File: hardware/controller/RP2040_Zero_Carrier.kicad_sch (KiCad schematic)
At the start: 2 parts, among them J1 20P 1.0mm FFC Type A, U1 Waveshare RP2040-Zero 23.5x18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

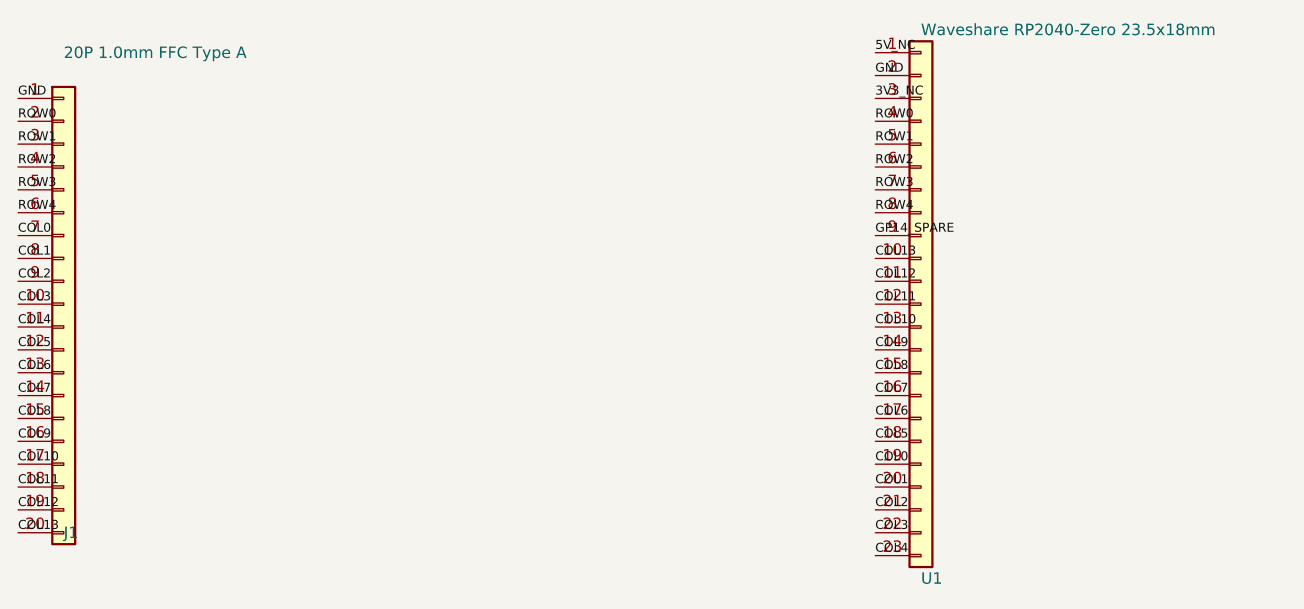
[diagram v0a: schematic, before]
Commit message: Finalize FFC routing and assembly-safe hardware
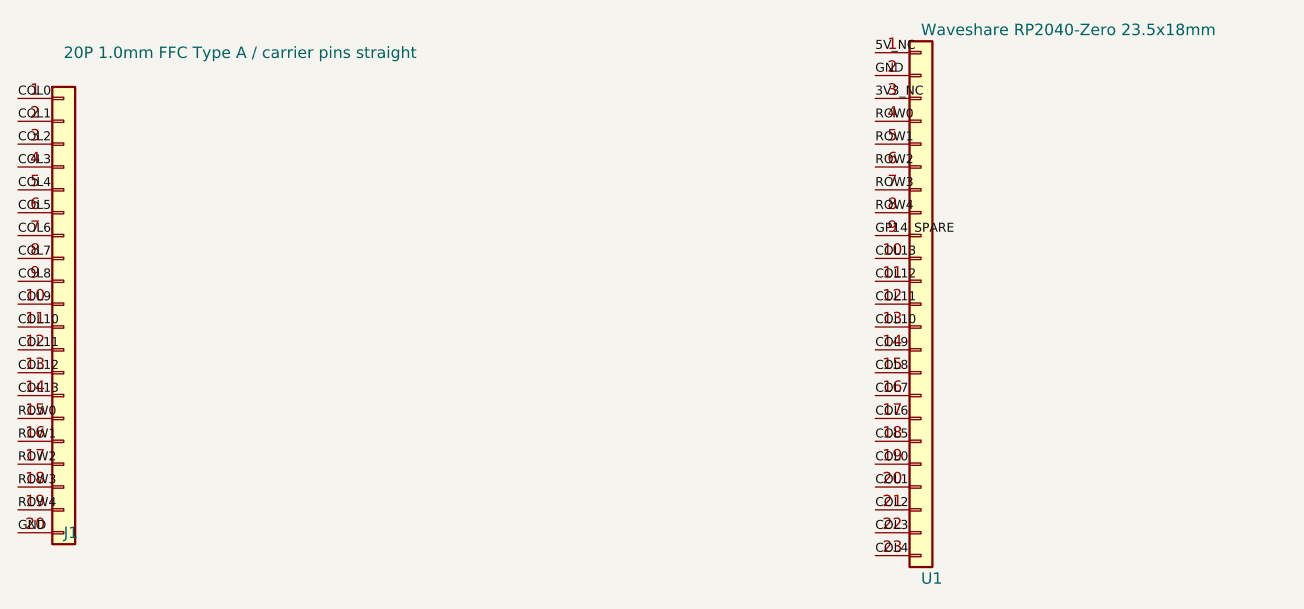
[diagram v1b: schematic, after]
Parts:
- J1: value 20P 1.0mm FFC Type A -> 20P 1.0mm FFC Type A / carrier pins straight
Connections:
- net COL0: now also J1.1 (Pin_1); no longer J1.7 (Pin_7)
- net COL1: now also J1.2 (Pin_2); no longer J1.8 (Pin_8)
- net COL10: now also J1.11 (Pin_11); no longer J1.17 (Pin_17)
- net COL11: now also J1.12 (Pin_12); no longer J1.18 (Pin_18)
- net COL12: now also J1.13 (Pin_13); no longer J1.19 (Pin_19)
- net COL13: now also J1.14 (Pin_14); no longer J1.20 (Pin_20)
- net COL2: now also J1.3 (Pin_3); no longer J1.9 (Pin_9)
- net COL3: now also J1.4 (Pin_4); no longer J1.10 (Pin_10)
- net COL4: now also J1.5 (Pin_5); no longer J1.11 (Pin_11)
- net COL5: now also J1.6 (Pin_6); no longer J1.12 (Pin_12)
- net COL6: now also J1.7 (Pin_7); no longer J1.13 (Pin_13)
- net COL7: now also J1.8 (Pin_8); no longer J1.14 (Pin_14)
- net COL8: now also J1.9 (Pin_9); no longer J1.15 (Pin_15)
- net COL9: now also J1.10 (Pin_10); no longer J1.16 (Pin_16)
- net GND: now also J1.20 (Pin_20); no longer J1.1 (Pin_1)
- net ROW0: now also J1.15 (Pin_15); no longer J1.2 (Pin_2)
- net ROW1: now also J1.16 (Pin_16); no longer J1.3 (Pin_3)
- net ROW2: now also J1.17 (Pin_17); no longer J1.4 (Pin_4)
- net ROW3: now also J1.18 (Pin_18); no longer J1.5 (Pin_5)
- net ROW4: now also J1.19 (Pin_19); no longer J1.6 (Pin_6)
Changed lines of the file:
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@@
 			)
 		)
-		(property "Value" "20P 1.0mm FFC Type A"
+		(property "Value" "20P 1.0mm FFC Type A / carrier pins straight"
 			(at 44.45 72.39 0.0000)
 			(effects
@@
 		(instances
 			(project "Minilite64 RP2040-Zero carrier"
-				(path "/281aadff-97dc-4c5d-822a-491d4e866b42"
+				(path "/44f8c00c-14ab-4b52-8662-688700ab1df1"
 					(reference "J1")
 					(unit 1)
@@
 		(instances
 			(project "Minilite64 RP2040-Zero carrier"
-				(path "/281aadff-97dc-4c5d-822a-491d4e866b42"
+				(path "/44f8c00c-14ab-4b52-8662-688700ab1df1"
 					(reference "U1")
 					(unit 1)
@@
 		)
 	)
+	(label "COL0"
+		(at 39.37 77.47 180)
+		(effects
+			(font
+				(size 1 1)
+			)
+			(justify left bottom)
+		)
+	)
+	(label "COL1"
+		(at 39.37 80.01 180)
+		(effects
+			(font
+				(size 1 1)
+			)
+			(justify left bottom)
+		)
+	)
+	(label "COL2"
+		(at 39.37 82.55 180)
+		(effects
+			(font
+				(size 1 1)
+			)
+			(justify left bottom)
+		)
+	)
+	(label "COL3"
+		(at 39.37 85.09 180)
+		(effects
+			(font
+				(size 1 1)
+			)
+			(justify left bottom)
+		)
+	)
+	(label "COL4"
+		(at 39.37 87.63 180)
+		(effects
+			(font
+				(size 1 1)
+			)
+			(justify left bottom)
+		)
+	)
+	(label "COL5"
+		(at 39.37 90.17 180)
+		(effects
+			(font
+				(size 1 1)
+			)
+			(justify left bottom)
+		)
+	)
+	(label "COL6"
+		(at 39.37 92.71 180)
+		(effects
+			(font
+				(size 1 1)
+			)
+			(justify left bottom)
+		)
+	)
+	(label "COL7"
+		(at 39.37 95.25 180)
+		(effects
+			(font
+				(size 1 1)
+			)
+			(justify left bottom)
+		)
+	)
+	(label "COL8"
+		(at 39.37 97.79 180)
+		(effects
+			(font
+				(size 1 1)
+			)
+			(justify left bottom)
+		)
+	)
+	(label "COL9"
+		(at 39.37 100.33 180)
+		(effects
+			(font
+				(size 1 1)
+			)
+			(justify left bottom)
+		)
+	)
+	(label "COL10"
+		(at 39.37 102.87 180)
+		(effects
+			(font
+				(size 1 1)
+			)
+			(justify left bottom)
+		)
+	)
+	(label "COL11"
+		(at 39.37 105.41 180)
+		(effects
+			(font
+				(size 1 1)
+			)
+			(justify left bottom)
+		)
+	)
+	(label "COL12"
+		(at 39.37 107.95 180)
+		(effects
+			(font
+				(size 1 1)
+			)
+			(justify left bottom)
+		)
+	)
+	(label "COL13"
+		(at 39.37 110.49 180)
+		(effects
+			(font
+				(size 1 1)
+			)
+			(justify left bottom)
+		)
+	)
+	(label "ROW0"
+		(at 39.37 113.03 180)
+		(effects
+			(font
+				(size 1 1)
+			)
+			(justify left bottom)
+		)
+	)
+	(label "ROW1"
+		(at 39.37 115.57 180)
+		(effects
+			(font
+				(size 1 1)
+			)
+			(justify left bottom)
+		)
+	)
+	(label "ROW2"
+		(at 39.37 118.11 180)
+		(effects
+			(font
+				(size 1 1)
+			)
+			(justify left bottom)
+		)
+	)
+	(label "ROW3"
+		(at 39.37 120.65 180)
+		(effects
+			(font
+				(size 1 1)
+			)
+			(justify left bottom)
+		)
+	)
+	(label "ROW4"
+		(at 39.37 123.19 180)
+		(effects
+			(font
+				(size 1 1)
+			)
+			(justify left bottom)
+		)
+	)
 	(label "GND"
-		(at 39.37 77.47 180)
-		(effects
-			(font
-				(size 1 1)
-			)
-			(justify left bottom)
-		)
-	)
-	(label "ROW0"
-		(at 39.37 80.01 180)
-		(effects
-			(font
-				(size 1 1)
-			)
-			(justify left bottom)
-		)
-	)
-	(label "ROW1"
-		(at 39.37 82.55 180)
-		(effects
-			(font
-				(size 1 1)
-			)
-			(justify left bottom)
-		)
-	)
-	(label "ROW2"
-		(at 39.37 85.09 180)
-		(effects
-			(font
-				(size 1 1)
-			)
-			(justify left bottom)
-		)
-	)
-	(label "ROW3"
-		(at 39.37 87.63 180)
-		(effects
-			(font
-				(size 1 1)
-			)
-			(justify left bottom)
-		)
-	)
-	(label "ROW4"
-		(at 39.37 90.17 180)
-		(effects
-			(font
-				(size 1 1)
-			)
-			(justify left bottom)
-		)
-	)
-	(label "COL0"
-		(at 39.37 92.71 180)
-		(effects
-			(font
-				(size 1 1)
-			)
-			(justify left bottom)
-		)
-	)
-	(label "COL1"
-		(at 39.37 95.25 180)
-		(effects
-			(font
-				(size 1 1)
-			)
-			(justify left bottom)
-		)
-	)
-	(label "COL2"
-		(at 39.37 97.79 180)
-		(effects
-			(font
-				(size 1 1)
-			)
-			(justify left bottom)
-		)
-	)
-	(label "COL3"
-		(at 39.37 100.33 180)
-		(effects
-			(font
-				(size 1 1)
-			)
-			(justify left bottom)
-		)
-	)
-	(label "COL4"
-		(at 39.37 102.87 180)
-		(effects
-			(font
-				(size 1 1)
-			)
-			(justify left bottom)
-		)
-	)
-	(label "COL5"
-		(at 39.37 105.41 180)
-		(effects
-			(font
-				(size 1 1)
-			)
-			(justify left bottom)
-		)
-	)
-	(label "COL6"
-		(at 39.37 107.95 180)
-		(effects
-			(font
-				(size 1 1)
-			)
-			(justify left bottom)
-		)
-	)
-	(label "COL7"
-		(at 39.37 110.49 180)
-		(effects
-			(font
-				(size 1 1)
-			)
-			(justify left bottom)
-		)
-	)
-	(label "COL8"
-		(at 39.37 113.03 180)
-		(effects
-			(font
-				(size 1 1)
-			)
-			(justify left bottom)
-		)
-	)
-	(label "COL9"
-		(at 39.37 115.57 180)
-		(effects
-			(font
-				(size 1 1)
-			)
-			(justify left bottom)
-		)
-	)
-	(label "COL10"
-		(at 39.37 118.11 180)
-		(effects
-			(font
-				(size 1 1)
-			)
-			(justify left bottom)
-		)
-	)
-	(label "COL11"
-		(at 39.37 120.65 180)
-		(effects
-			(font
-				(size 1 1)
-			)
-			(justify left bottom)
-		)
-	)
-	(label "COL12"
-		(at 39.37 123.19 180)
-		(effects
-			(font
-				(size 1 1)
-			)
-			(justify left bottom)
-		)
-	)
-	(label "COL13"
 		(at 39.37 125.73 180)
 		(effects
